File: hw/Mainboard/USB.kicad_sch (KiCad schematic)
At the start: 3 parts, among them J14 USB2.0_HOST_TYPE_C

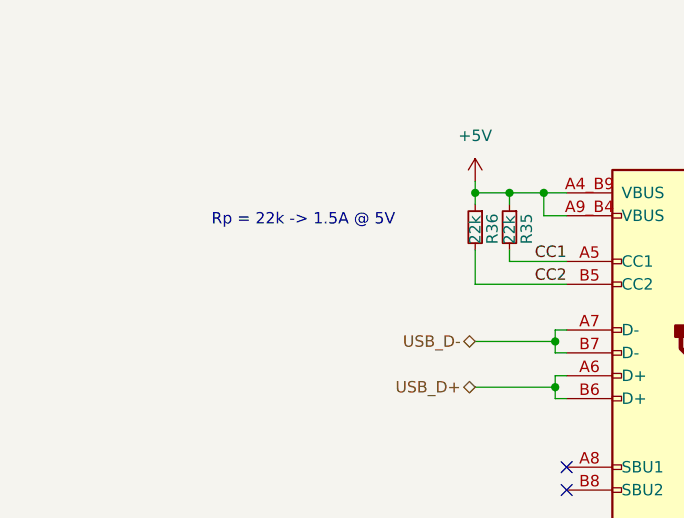
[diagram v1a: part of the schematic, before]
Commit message: hw: USB CC1/CC2 = 56k
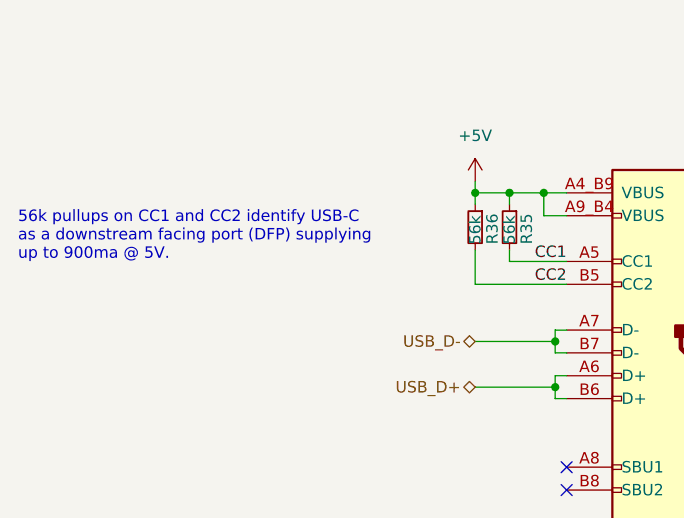
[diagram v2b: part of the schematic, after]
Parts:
- R35, R36: value 22k -> 56k; LCSC C25768 -> C25796
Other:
- note added: "56k pullups on CC1 and CC2 identify USB-C as a downstream facing port (DFP) supplying up to 900ma @ 5V."
- note removed: "Rp = 22k -> 1.5A @ 5V"
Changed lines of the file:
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@@
     (effects (font (size 4 4)) (justify right bottom))
   )
-  (text "Rp = 22k -> 1.5A @ 5V" (at 118.11 78.74 180)
-    (effects (font (size 1.27 1.27)) (justify right bottom))
+  (text "56k pullups on CC1 and CC2 identify USB-C\nas a downstream facing port (DFP) supplying\nup to 900ma @ 5V."
+    (at 76.2 82.55 0)
+    (effects (font (size 1.27 1.27)) (justify left bottom))
   )
   (label "CC2" (at 137.16 85.09 180)
@@
       (effects (font (size 1.27 1.27)) (justify left))
     )
-    (property "Value" "22k" (id 1) (at 127 80.645 90)
+    (property "Value" "56k" (id 1) (at 127 80.645 90)
       (effects (font (size 1.27 1.27)) (justify left))
     )
@@
       (effects (font (size 1.27 1.27)) hide)
     )
-    (property "Datasheet" "https://datasheet.lcsc.com/lcsc/2206010100_UNI-ROYAL-Uniroyal-Elec-0402WGF2202TCE_C25768.pdf" (id 3) (at 127 78.74 0)
+    (property "Datasheet" "" (id 3) (at 127 78.74 0)
       (effects (font (size 1.27 1.27)) hide)
     )
-    (property "LCSC" "C25768" (id 4) (at 127 78.74 0)
+    (property "LCSC" "C25796" (id 4) (at 127 78.74 0)
       (effects (font (size 1.27 1.27)) hide)
     )
@@
   (symbol (lib_id "power:+5V") (at 127 73.66 0) (mirror y) (unit 1)
     (in_bom yes) (on_board yes) (fields_autoplaced)
-    (property "Reference" "#PWR?" (id 0) (at 127 77.47 0)
+    (property "Reference" "#PWR045" (id 0) (at 127 77.47 0)
       (effects (font (size 1.27 1.27)) hide)
     )
@@
       (effects (font (size 1.27 1.27)) (justify left))
     )
-    (property "Value" "22k" (id 1) (at 130.81 80.645 90)
+    (property "Value" "56k" (id 1) (at 130.81 80.645 90)
       (effects (font (size 1.27 1.27)) (justify left))
     )
@@
       (effects (font (size 1.27 1.27)) hide)
     )
-    (property "Datasheet" "https://datasheet.lcsc.com/lcsc/2206010100_UNI-ROYAL-Uniroyal-Elec-0402WGF2202TCE_C25768.pdf" (id 3) (at 130.81 78.74 0)
+    (property "Datasheet" "" (id 3) (at 130.81 78.74 0)
       (effects (font (size 1.27 1.27)) hide)
     )
-    (property "LCSC" "C25768" (id 4) (at 130.81 78.74 0)
+    (property "LCSC" "C25796" (id 4) (at 130.81 78.74 0)
       (effects (font (size 1.27 1.27)) hide)
     )
@@
   (symbol (lib_id "power:GND") (at 154.94 119.38 0) (unit 1)
     (in_bom yes) (on_board yes)
-    (property "Reference" "#PWR?" (id 0) (at 154.94 125.73 0)
+    (property "Reference" "#PWR066" (id 0) (at 154.94 125.73 0)
       (effects (font (size 1.27 1.27)) hide)
     )

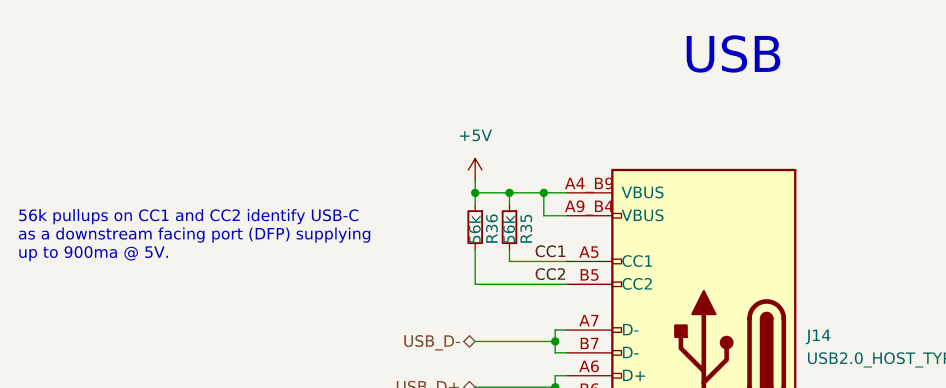
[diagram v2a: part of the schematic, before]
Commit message: hw: Use 74HC154 for keyboard
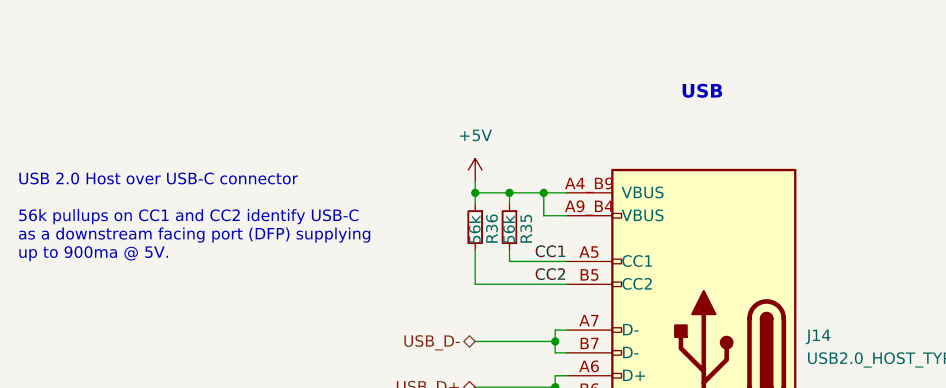
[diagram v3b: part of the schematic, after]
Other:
- note added: "USB 2.0 Host over USB-C connector 56k pullups on CC1 and CC2 identify USB-C as a downstream facing port (DFP) supplying up to 900ma @ 5V."
- note removed: "56k pullups on CC1 and CC2 identify USB-C as a downstream facing port (DFP) supplying up to 900ma @ 5V."
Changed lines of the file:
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@@
     (stroke (width 0) (type default) (color 0 0 0 0))
   )
-  (text "USB" (at 161.29 62.23 180)
-    (effects (font (size 4 4)) (justify right bottom))
-  )
-  (text "56k pullups on CC1 and CC2 identify USB-C\nas a downstream facing port (DFP) supplying\nup to 900ma @ 5V."
+  (text "USB 2.0 Host over USB-C connector\n\n56k pullups on CC1 and CC2 identify USB-C\nas a downstream facing port (DFP) supplying\nup to 900ma @ 5V."
     (at 76.2 82.55 0)
     (effects (font (size 1.27 1.27)) (justify left bottom))
   )
+  (text "USB" (at 149.86 64.77 0)
+    (effects (font (size 1.5 1.5) (thickness 0.8) bold) (justify left bottom))
+  )
   (label "CC2" (at 137.16 85.09 180)

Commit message: hw: wip
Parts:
- added PT10, PT11, PT19, PT20: PowerTie_2, PET:NetTie-2_SMD_Pad_1.6_to_0.4mm, symbol PET:PowerTie_2
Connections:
- net +5V: now also PT19.1, PT20.1; no longer J14.A4_B9 (VBUS), J14.A9_B4 (VBUS), R35.1, R36.1
- net GND: no longer J14.A12_B1 (GND), J14.A1_B12 (GND)
- new net: J14.A4_B9 (VBUS), PT19.2, R35.1
- new net: J14.A12_B1 (GND), PT10.2
- new net: J14.A1_B12 (GND), PT11.2
- new net: J14.A9_B4 (VBUS), PT20.2, R36.1
- new net PD_GND: PT10.1, PT11.1
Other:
- moved on the sheet: R35, R36

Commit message: hw: update 10u caps
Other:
- title: (none) -> CBM PET Mainboard Replacement
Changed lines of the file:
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@@
 (kicad_sch (version 20211123) (generator eeschema)
-  (paper "A4")
+  (paper "A")
+  (title_block
+    (title "CBM PET Mainboard Replacement")
+  )
   (junction (at 129.54 73.66) (diameter 0) (color 0 0 0 0)
   )

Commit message: hw: wip
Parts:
- added J8: BOOTSEL, Connector_PinHeader_2.54mm:PinHeader_1x04_P2.54mm_Vertical, symbol Connector:Conn_01x04_Male
- added R73, R74: 5k1, Resistor_SMD:R_0402_1005Metric, symbol Device:R_Small
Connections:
- net +5V: now also J8.4 (Pin_4); no longer PT19.1, PT20.1
- net CC1: now also R74.1
- net CC2: now also R73.1
- net GND: now also J8.1 (Pin_1)
- new net: J8.3 (Pin_3), PT19.1, PT20.1
- new net BOOTSEL: J8.2 (Pin_2), R73.2, R74.2
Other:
- note added: "USB 2.0 Host over USB-C connector As a host, the 56k pullups on CC1 and CC2 identify USB-C as a power source supplying up to 900ma @ 5V. When flashing the MCU, the 5.1k pulldowns on CC1 and CC2 identify USB-C as a power consumer."
- note removed: "USB"
- note removed: "USB 2.0 Host over USB-C connector 56k pullups on CC1 and CC2 identify USB-C as a downstream facing port (DFP) supplying up to 900ma @ 5V."
- moved on the sheet: R35, R36
